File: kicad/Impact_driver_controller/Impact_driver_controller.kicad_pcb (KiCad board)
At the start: 2 copper layers, 36 parts, among them U1 DRV8874_module, U10 Control_panel_module, U2 ACS712 30A, U3 LM78M05, U4 DRV8874_module, U5 DRV8874_module, U6 MCU_module, U7 DRV8874_module, U8 DRV8874_module, U9 DRV8874_module

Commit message: First main board layout
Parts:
- R4: footprint Resistor_SMD:R_1206_3216Metric_Pad1.30x1.75mm_HandSolder -> Resistor_SMD:R_0603_1608Metric_Pad0.98x0.95mm_HandSolder
- moved U9 191.2 mm to (228.5, 100.0), turned to -90 degrees
- moved D8 183.8 mm to (230.2, 124.6), turned to 180 degrees
- moved R10 176.5 mm to (225.9, 124.6)
- moved D7 164.4 mm to (205.7, 124.6), turned to 180 degrees
- moved U8 161.5 mm to (203.9, 100.0), turned to -90 degrees
- moved R9 157.5 mm to (201.4, 124.6)
- moved D6 146.5 mm to (181.2, 124.6), turned to 180 degrees
- moved R8 140.2 mm to (176.9, 124.6)
- moved U7 134.1 mm to (179.4, 100.0), turned to -90 degrees
- moved D5 130.7 mm to (156.6, 124.6), turned to 180 degrees
- moved R7 125.3 mm to (152.2, 124.6)
- moved D3 118.2 mm to (132.1, 124.6), turned to 180 degrees
- moved R6 113.9 mm to (127.7, 124.6)
- moved U5 111.0 mm to (154.8, 100.0), turned to -90 degrees
- moved D1 109.7 mm to (107.5, 124.6), turned to 180 degrees
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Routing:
- added copper zone on F.Cu, net +VDD
- added copper zone on F.Cu, net /Current probe/IN
- added copper zone on B.Cu, net /Power supply/+V_IN
- added copper zone on B.Cu, net GND
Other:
- board outline added: 208.2 x 101.1 mm

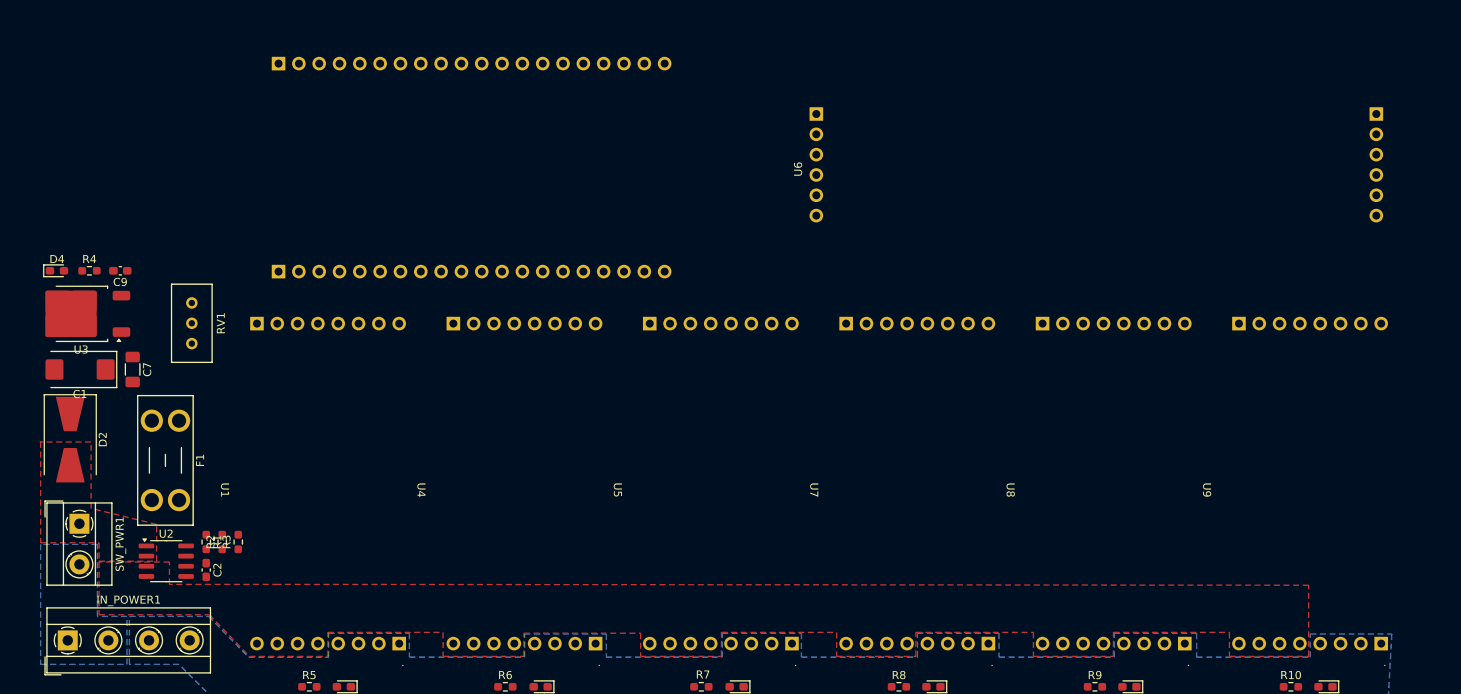
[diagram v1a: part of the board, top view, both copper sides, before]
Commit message: Main board wiring
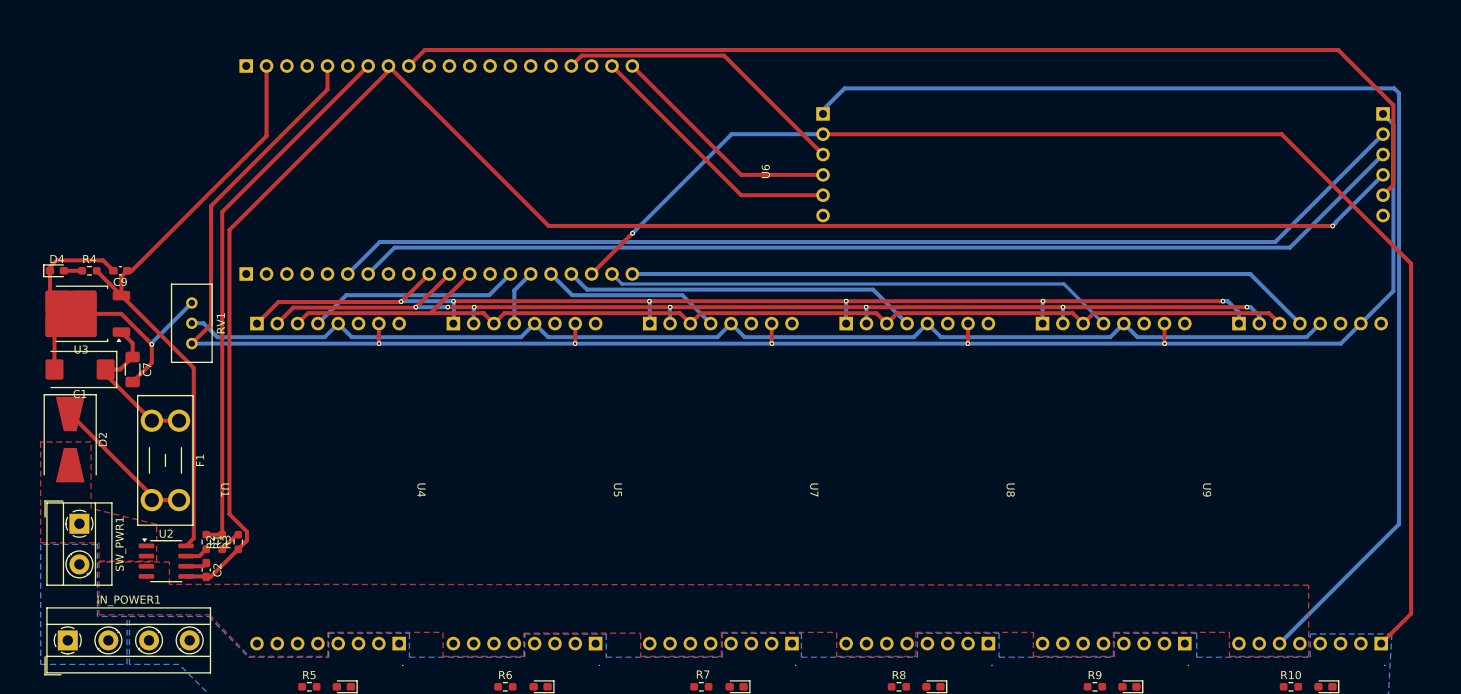
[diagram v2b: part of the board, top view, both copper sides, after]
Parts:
- moved U6 4.05 mm to (124.7, 60.1)
- moved U10 0.84 mm to (203.6, 59.9)
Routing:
- net +3.3V: track 0.00 -> 229.9 mm, vias 0 -> 5
- net AGND: track 0.00 -> 213.3 mm, vias 0 -> 1
- net GND: track 0.00 -> 211.4 mm, vias 0 -> 2
- net /Drivers/+Vref: track 0.00 -> 149.5 mm
- net +VDD: track 0.00 -> 148.8 mm
- net /Drivers/EN: track 0.00 -> 142.2 mm, vias 0 -> 6
- net /Drivers/PH: track 0.00 -> 139.2 mm, vias 0 -> 7
- net Net-(U10-RV_SPEED): track 0.00 -> 138.6 mm
- net SDA: track 0.00 -> 136.6 mm
- net /Drivers/SLEEP: track 0.00 -> 135.1 mm
- net SCL: track 0.00 -> 133.0 mm
- net /Drivers/FAULT_6: track 0.00 -> 86.0 mm
- net +5V: track 0.00 -> 76.4 mm
- net /Current probe/I_MEAS: track 0.00 -> 68.1 mm
- net /Drivers/FAULT_5: track 0.00 -> 64.0 mm
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
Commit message: main board silkscreen
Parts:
- added G***: LOGO, LOGO, F.Cu at (85.0, 58.7)
- added H3: MountingHole, MountingHole:MountingHole_3.2mm_M3, F.Cu at (66.0, 47.0)
- added H3: MountingHole, MountingHole:MountingHole_3.2mm_M3, F.Cu at (244.0, 47.0)
- added H3: MountingHole, MountingHole:MountingHole_3.2mm_M3, F.Cu at (66.0, 124.0)
- added H3: MountingHole, MountingHole:MountingHole_3.2mm_M3, F.Cu at (244.0, 124.0)
- renumbered D5 to ERROR, D3 to ERROR, D6 to ERROR, D8 to ERROR, D7 to ERROR, D1 to ERROR, D4 to POWER
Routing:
- net GND: track 211.4 -> 327.1 mm, vias 2 -> 57
- net /Drivers/FAULT_1: track 26.6 -> 89.1 mm, vias 0 -> 2
- net /Drivers/FAULT_5: track 64.0 -> 120.5 mm, vias 0 -> 2
- net /Drivers/FAULT_6: track 86.0 -> 142.2 mm, vias 0 -> 2
- net /Drivers/FAULT_4: track 44.5 -> 100.5 mm, vias 0 -> 2
- net /Drivers/FAULT_2: track 7.05 -> 62.4 mm, vias 0 -> 2
- net /Drivers/FAULT_3: track 22.5 -> 77.6 mm, vias 0 -> 2
- net Net-(D5-A): track 0.00 -> 2.62 mm
- net Net-(D3-A): track 0.00 -> 2.62 mm
- net Net-(D1-A): track 0.00 -> 2.53 mm
- net Net-(D8-A): track 0.00 -> 2.52 mm
- net Net-(D7-A): track 0.00 -> 2.52 mm
- net Net-(D6-A): track 0.00 -> 2.52 mm
- net +VDD: track 148.8 -> 146.9 mm, vias 0 -> 28
- net /Current probe/IN: vias 0 -> 10
- added copper zone on B.Cu, net (none)
- added copper zone on F.Cu, net (none)
- added copper zone on B.Cu, net +VDD
- added copper zone on B.Cu, net /Current probe/IN
- added copper zone on F.Cu, net /Power supply/+V_IN
- added copper zone on F.Cu, net GND
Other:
- board size 208.2 x 101.1 mm -> 185 x 84.5 mm
- board text added: "+24V"
- board text added: "DRV8874 module"
- board text added: "GND"
- board text added: "Impact driver controller v1.0.0"
- board text added: "MCU module"
- board text added: "PWR SWITCH"
- board text added: "control panel module"

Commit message: dots for orientation
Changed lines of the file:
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@@
 		(sheetfile "Drivers.kicad_sch")
 		(attr through_hole)
+		(fp_circle
+			(center 16.125 -10.075)
+			(end 17.125 -10.075)
+			(stroke
+				(width 0.1)
+				(type solid)
+			)
+			(fill solid)
+			(layer "F.SilkS")
+		)
 		(fp_line
 			(start 19.425 11.83)
@@
 		)
 		(property "Value" "DRV8874_module"
-			(at 0 14.6 270)
+			(at 0 14.6 -90)
 			(unlocked yes)
 			(layer "F.Fab")
@@
 		(sheetfile "Drivers.kicad_sch")
 		(attr through_hole)
+		(fp_circle
+			(center 16.125 -10.075)
+			(end 17.125 -10.075)
+			(stroke
+				(width 0.1)
+				(type solid)
+			)
+			(fill solid)
+			(layer "F.SilkS")
+		)
 		(fp_line
 			(start 19.425 11.83)
@@
 		(sheetfile "Drivers.kicad_sch")
 		(attr through_hole)
+		(fp_circle
+			(center 16.125 -10.075)
+			(end 17.125 -10.075)
+			(stroke
+				(width 0.1)
+				(type solid)
+			)
+			(fill solid)
+			(layer "F.SilkS")
+		)
 		(fp_line
 			(start 19.425 11.83)
@@
 		(sheetfile "Drivers.kicad_sch")
 		(attr through_hole)
+		(fp_circle
+			(center 16.125 -10.075)
+			(end 17.125 -10.075)
+			(stroke
+				(width 0.1)
+				(type solid)
+			)
+			(fill solid)
+			(layer "F.SilkS")
+		)
 		(fp_line
 			(start 19.425 11.83)
@@
 		(sheetfile "Impact_driver_controller.kicad_sch")
 		(attr through_hole)
+		(fp_circle
+			(center -36.275 -11.3)
+			(end -35.275 -11.3)
+			(stroke
+				(width 0.1)
+				(type solid)
+			)
+			(fill solid)
+			(layer "F.SilkS")
+		)
 		(fp_line
 			(start -38.7 -10.9)
@@
 		(sheetfile "Drivers.kicad_sch")
 		(attr through_hole)
+		(fp_circle
+			(center 16.125 -10.075)
+			(end 17.125 -10.075)
+			(stroke
+				(width 0.1)
+				(type solid)
+			)
+			(fill solid)
+			(layer "F.SilkS")
+		)
 		(fp_line
 			(start 19.425 11.83)
@@
 		(sheetfile "Impact_driver_controller.kicad_sch")
 		(attr through_hole)
+		(fp_circle
+			(center 14.15 30.925)
+			(end 15.15 30.925)
+			(stroke
+				(width 0.1)
+				(type solid)
+			)
+			(fill solid)
+			(layer "F.SilkS")
+		)
 		(fp_line
 			(start 16.77 -30.8)
@@
 		(sheetfile "Drivers.kicad_sch")
 		(attr through_hole)
+		(fp_circle
+			(center 16.125 -10.075)
+			(end 17.125 -10.075)
+			(stroke
+				(width 0.1)
+				(type solid)
+			)
+			(fill solid)
+			(layer "F.SilkS")
+		)
 		(fp_line
 			(start 19.425 11.83)

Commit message: Connector for bigger current, control module 2
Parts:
- removed IN_POWER1: Screw_Terminal_01x04, TerminalBlock_MetzConnect:TerminalBlock_MetzConnect_Type101_RT01604HBWC_1x04_P5.08mm_Horizontal
- removed SW_PWR1: Screw_Terminal_01x02, TerminalBlock_MetzConnect:TerminalBlock_MetzConnect_Type101_RT01602HBWC_1x02_P5.08mm_Horizontal
- added POWER_INPUT1: +24 V, T-DEAN_impact:DEANS, F.Cu at (81.7, 119.9)
- added PWR_BUTTON1: ~, T-DEAN_impact:DEANS, F.Cu at (73.3, 105.7)
- renumbered ERROR to D1, ERROR to D3, POWER to D4, ERROR to D5, ERROR to D6, ERROR to D7, ERROR to D8
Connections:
- U10 pad 12: unconnected-(U10-none-Pad12) -> Net-(U10-RV2)
- U6 pad 31: unconnected-(U6-F0-Pad31) -> Net-(U10-RV2)
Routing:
- net Net-(U10-RV2): track 0.00 -> 127.0 mm, vias 0 -> 1
- net /Current probe/IN: vias 10 -> 7

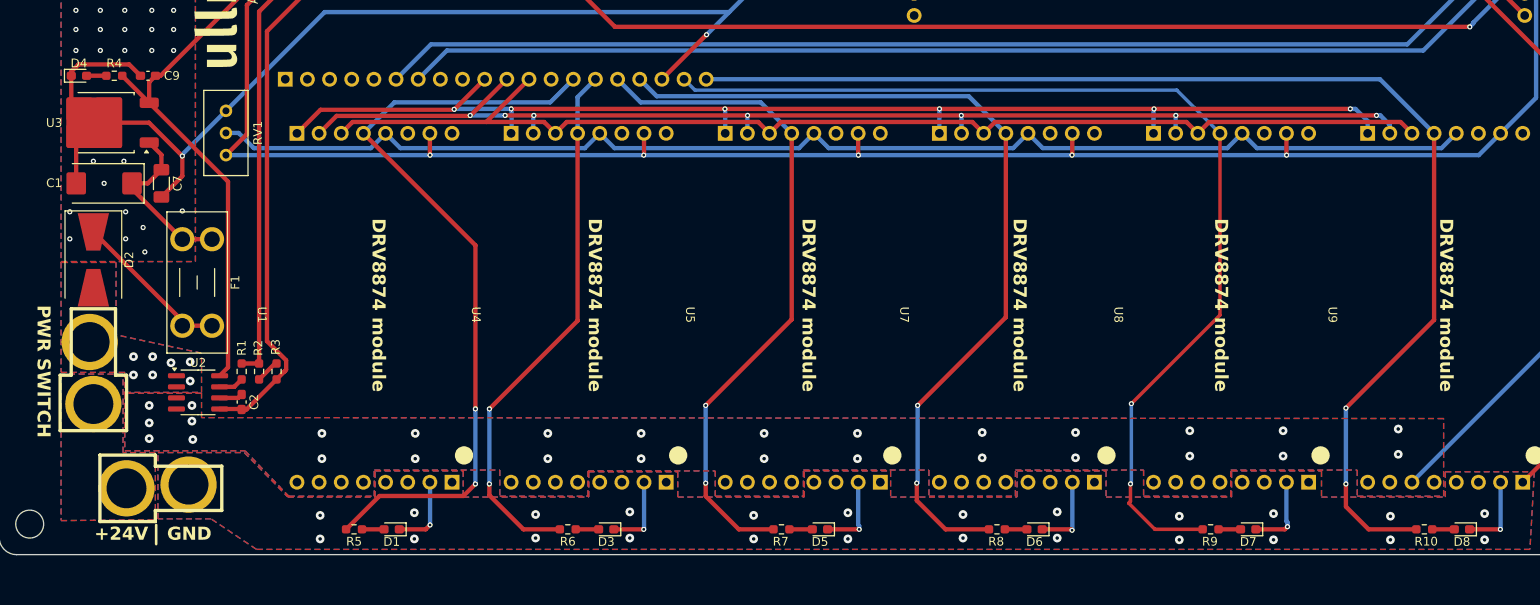
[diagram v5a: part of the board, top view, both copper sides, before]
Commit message: LED footprint update
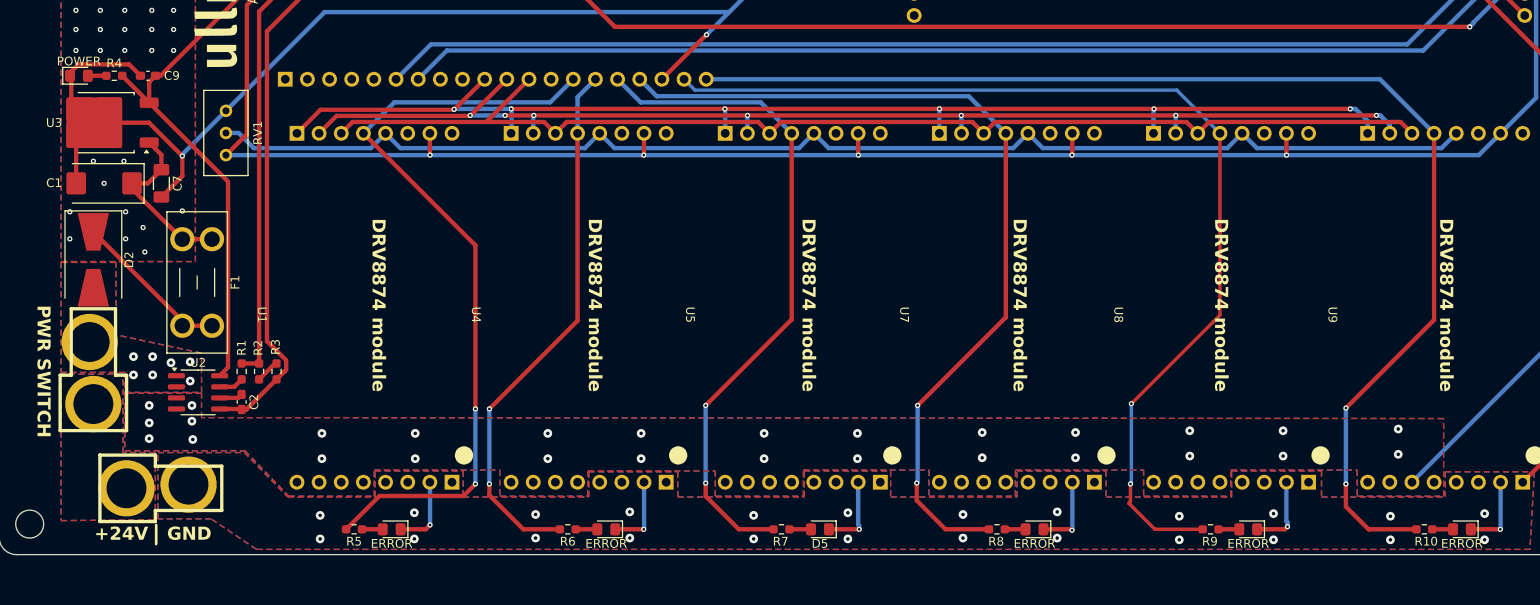
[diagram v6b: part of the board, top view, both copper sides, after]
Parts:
- C1: value 100 uF, 25V -> 100uF
- D5: footprint LED_SMD:LED_0603_1608Metric_Pad1.05x0.95mm_HandSolder -> LED_SMD:LED_0805_2012Metric_Pad1.15x1.40mm_HandSolder
- ERROR: renamed from D3; footprint LED_SMD:LED_0603_1608Metric_Pad1.05x0.95mm_HandSolder -> LED_SMD:LED_0805_2012Metric_Pad1.15x1.40mm_HandSolder
- ERROR: renamed from D6; footprint LED_SMD:LED_0603_1608Metric_Pad1.05x0.95mm_HandSolder -> LED_SMD:LED_0805_2012Metric_Pad1.15x1.40mm_HandSolder
- ERROR: renamed from D8; footprint LED_SMD:LED_0603_1608Metric_Pad1.05x0.95mm_HandSolder -> LED_SMD:LED_0805_2012Metric_Pad1.15x1.40mm_HandSolder
- ERROR: renamed from D7; footprint LED_SMD:LED_0603_1608Metric_Pad1.05x0.95mm_HandSolder -> LED_SMD:LED_0805_2012Metric_Pad1.15x1.40mm_HandSolder
- ERROR: renamed from D1; footprint LED_SMD:LED_0603_1608Metric_Pad1.05x0.95mm_HandSolder -> LED_SMD:LED_0805_2012Metric_Pad1.15x1.40mm_HandSolder
- F1: value 1 A -> FUSE 1A
- J1: renamed from POWER_INPUT1; value +24 V -> 1x2 TDEAN
- J2: renamed from PWR_BUTTON1; value ~ -> 1x2 TDEAN
- POWER: renamed from D4; footprint LED_SMD:LED_0603_1608Metric_Pad1.05x0.95mm_HandSolder -> LED_SMD:LED_0805_2012Metric_Pad1.15x1.40mm_HandSolder
- RV1: value W203 (100K) -> 100k
- U2: value ACS712 30A -> ACS71230A
